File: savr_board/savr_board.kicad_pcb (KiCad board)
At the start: 6 copper layers, 11 parts, among them J1 SATA-7, J2 SATA-7, J3 SATA-7, J4 SATA-7, U1 XC7Z030-CLG485, U2 DDR3_256Mx16, U3 DDR3_256Mx16

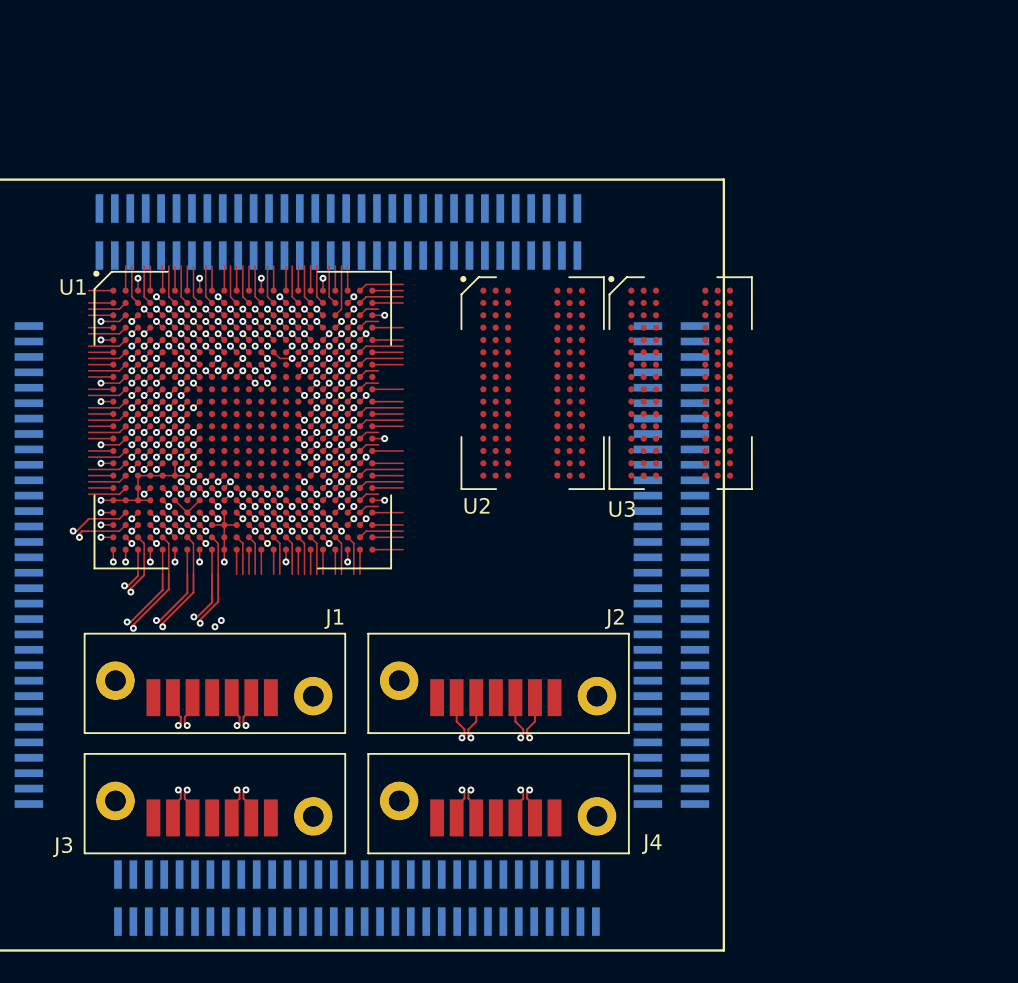
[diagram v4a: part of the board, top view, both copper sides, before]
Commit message: Did a bunch of escape reshuffling and managed to route the DDR address and control lines. This probably won't work though since A10 and A12 have dual functionality that the CPU might use.
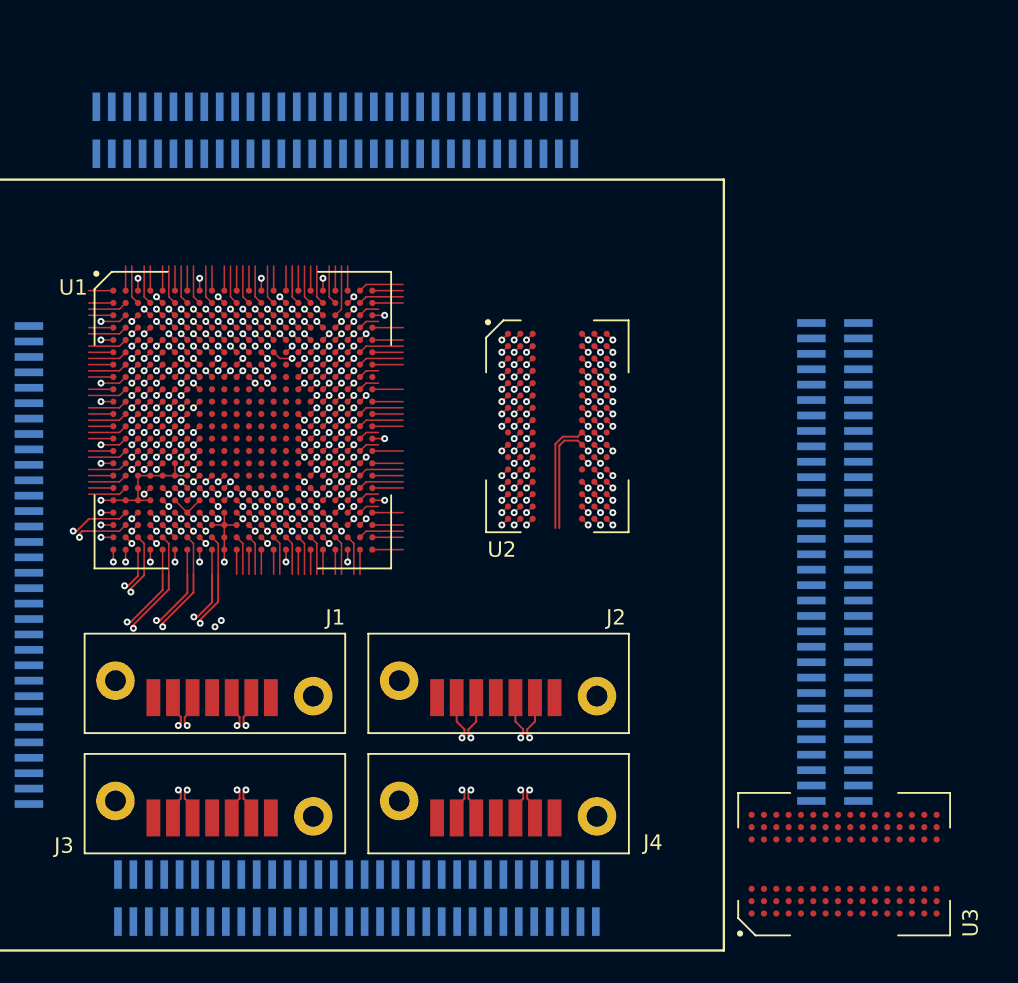
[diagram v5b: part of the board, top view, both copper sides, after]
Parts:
- moved U3 41.1 mm to (151.8, 147.6), turned to 90 degrees
- moved REF** 10.6 mm to (157.2, 124.8)
- moved REF** 6.60 mm to (124.8, 96.8)
- moved U2 3.22 mm to (136.0, 110.0)
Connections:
- net /RX0N renamed Net-(J1-Pad6)
- net /RX0P renamed Net-(J1-Pad5)
- net /RX1N renamed Net-(J2-Pad6)
- net /RX1P renamed Net-(J2-Pad5)
- net /RX2N renamed Net-(J3-Pad6)
- net /RX2P renamed Net-(J3-Pad5)
- net /RX3N renamed Net-(J4-Pad6)
- net /RX3P renamed Net-(J4-Pad5)
- net /TX0N renamed Net-(J1-Pad3)
- net /TX0P renamed Net-(J1-Pad2)
- net /TX1N renamed Net-(J2-Pad3)
- net /TX1P renamed Net-(J2-Pad2)
- net /TX2N renamed Net-(J3-Pad3)
- net /TX2P renamed Net-(J3-Pad2)
- net /TX3N renamed Net-(J4-Pad3)
- net /TX3P renamed Net-(J4-Pad2)
- U1 pad AA22: /DQ26 -> /DQ24
- U1 pad B21: /DQ2 -> /DQ0
- U1 pad C20: /DQ1 -> /DQ0
- U1 pad D20: /DQ3 -> /DQ0
- U1 pad E20: /DQ4 -> /DQ0
- U1 pad E22: /DQ5 -> /DQ0
- U1 pad F21: /DQ6 -> /DQ0
- U1 pad F22: /DQ7 -> /DQ0
- U1 pad G22: /DQ9 -> /DQ8
- U1 pad J22: /DQ14 -> /DQ8
- U1 pad K20: /DQ15 -> /DQ8
- U1 pad K22: /DQ13 -> /DQ8
- U1 pad L20: /DQ12 -> /DQ8
- U1 pad L21: /DQ11 -> /DQ8
- U1 pad L22: /DQ10 -> /DQ8
- U1 pad M21: /DQ22 -> /DQ16
- U1 pad N20: /DQ18 -> /DQ16
- U1 pad R20: /DQ20 -> /DQ16
- U1 pad R22: /DQ23 -> /DQ16
- U1 pad T20: /DQ17 -> /DQ16
- U1 pad T21: /DQ21 -> /DQ16
- U1 pad T22: /DQ19 -> /DQ16
- U1 pad U21: /DQ27 -> /DQ24
- U1 pad U22: /DQ25 -> /DQ24
- U1 pad V20: /DQ30 -> /DQ24
- U1 pad W20: /DQ29 -> /DQ24
- U1 pad W22: /DQ28 -> /DQ24
- U1 pad Y22: /DQ31 -> /DQ24
- U2 pad A2: /DQ13 -> /DQ8
- U2 pad A3: /DQ15 -> /DQ8
- U2 pad A7: /DQ12 -> /DQ8
- U2 pad B8: /DQ14 -> /DQ8
- U2 pad C2: /DQ11 -> /DQ8
- U2 pad C3: /DQ9 -> /DQ8
- U2 pad C8: /DQ10 -> /DQ8
- U2 pad F2: /DQ2 -> /DQ0
- U2 pad F7: /DQ1 -> /DQ0
- U2 pad F8: /DQ3 -> /DQ0
- U2 pad G2: /DQ6 -> /DQ0
- U2 pad H3: /DQ4 -> /DQ0
- U2 pad H7: /DQ7 -> /DQ0
- U2 pad H8: /DQ5 -> /DQ0
- U2 pad L7: /A10 -> /A6
- U2 pad N2: /A3 -> /A1
- U2 pad N3: /A0 -> /A4
- U2 pad N7: /A12 -> /A7
- U2 pad P2: /A5 -> /A3
- U2 pad P3: /A2 -> /A0
- U2 pad P7: /A1 -> /A11
- U2 pad P8: /A4 -> /A5
- U2 pad R2: /A7 -> /A10
- U2 pad R3: /A9 -> /A2
- U2 pad R7: /A11 -> /A13
- U2 pad R8: /A6 -> /A9
- U2 pad T3: /A13 -> /A8
- U2 pad T7: /A14 -> /A12
- U2 pad T8: /A8 -> /A14
- U3 pad A2: /DQ29 -> /DQ24
- U3 pad A3: /DQ31 -> /DQ24
- U3 pad A7: /DQ28 -> /DQ24
- U3 pad B8: /DQ30 -> /DQ24
- U3 pad C2: /DQ27 -> /DQ24
- U3 pad C3: /DQ25 -> /DQ24
- U3 pad C8: /DQ26 -> /DQ24
- U3 pad F2: /DQ18 -> /DQ16
- U3 pad F7: /DQ17 -> /DQ16
- U3 pad F8: /DQ19 -> /DQ16
- U3 pad G2: /DQ22 -> /DQ16
- U3 pad H3: /DQ20 -> /DQ16
- U3 pad H7: /DQ23 -> /DQ16
- U3 pad H8: /DQ21 -> /DQ16
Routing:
- net /BA1: track 7.13 -> 40.2 mm, vias 1 -> 2
- net /A5: track 6.33 -> 35.2 mm, vias 1 -> 2
- net /A7: track 7.53 -> 34.6 mm, vias 1 -> 2
- net /A6: track 8.33 -> 34.1 mm, vias 1 -> 2
- net /DQ0: track 2.00 -> 26.7 mm, vias 0 -> 11
- net /A9: track 6.33 -> 30.7 mm, vias 1 -> 2
- net /A11: track 6.33 -> 30.3 mm, vias 1 -> 2
- net /A14: track 5.13 -> 28.3 mm, vias 1 -> 2
- net /DQ8: track 2.97 -> 25.8 mm, vias 0 -> 10
- net /DQ16: track 2.00 -> 24.6 mm, vias 0 -> 3
- net /A13: track 5.13 -> 27.3 mm, vias 1 -> 2
- net /A12: track 5.13 -> 26.5 mm, vias 1 -> 2
- net /A10: track 4.17 -> 23.5 mm, vias 1 -> 2
- net /A8: track 6.33 -> 25.6 mm, vias 1 -> 2
- net /DQ24: track 4.33 -> 23.6 mm, vias 1 -> 3
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
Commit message: Pin swaps to support A10/A12 being the same. I don't like this much since I had to put them on a different layer.
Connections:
- U2 pad L7: /A6 -> /A10
- U2 pad N7: /A7 -> /A12
- U2 pad R2: /A10 -> /A6
- U2 pad T7: /A12 -> /A7
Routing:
- net /A10: track 23.5 -> 18.5 mm
- net /A12: track 26.5 -> 21.9 mm
- net /A6: track 34.1 -> 33.1 mm
- net /BA1: track 40.2 -> 41.1 mm

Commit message: More routing tests for DDR
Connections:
- U2 pad P7: /A11 -> /A7
- U2 pad P8: /A5 -> /A6
- U2 pad R2: /A6 -> /A8
- U2 pad R7: /A13 -> /A11
- U2 pad R8: /A9 -> /A5
- U2 pad T3: /A8 -> /A14
- U2 pad T7: /A7 -> /A13
- U2 pad T8: /A14 -> /A9
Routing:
- net /A6: track 33.1 -> 36.9 mm
- net /A14: track 28.6 -> 25.2 mm
- net /A13: track 27.6 -> 26.7 mm
- net /A7: track 34.5 -> 35.2 mm
- net /A8: track 25.6 -> 25.0 mm
